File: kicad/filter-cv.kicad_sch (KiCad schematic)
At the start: 21 parts, among them Q10 2N3904, Q11 2N3906, Q9 2N3906, U16 TL074

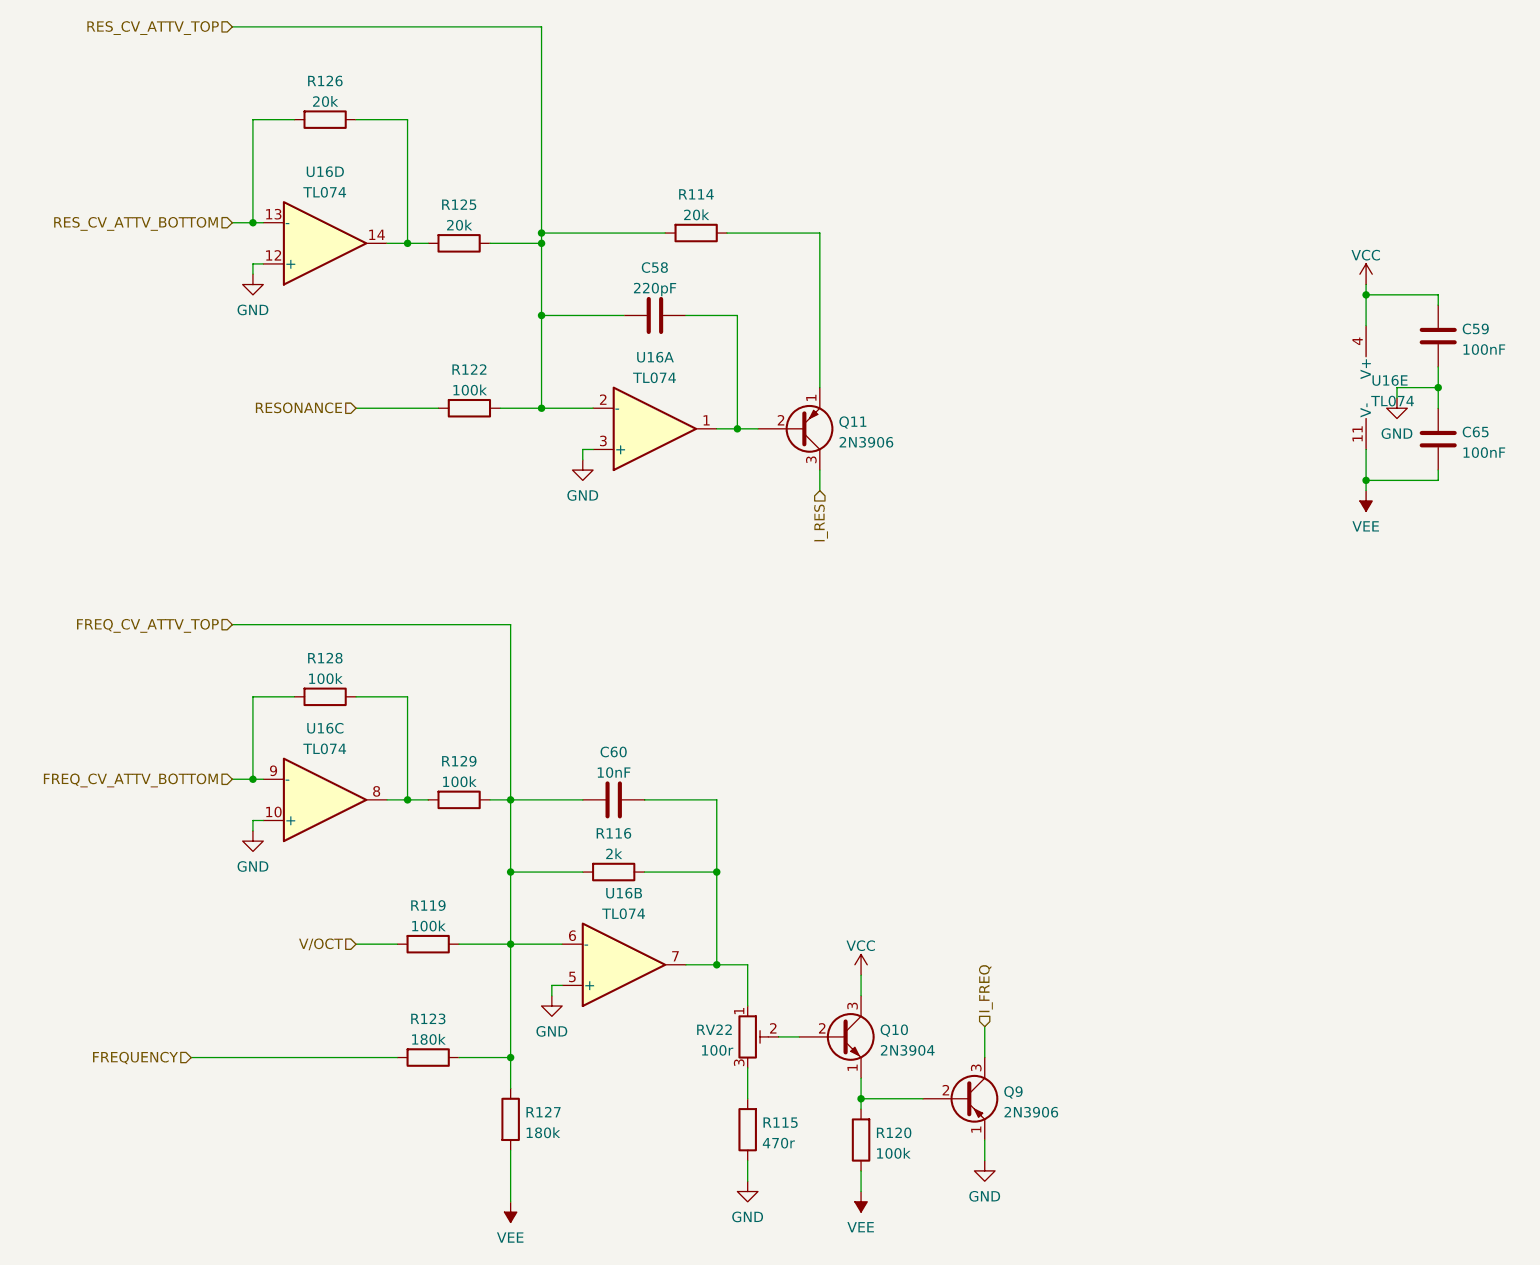
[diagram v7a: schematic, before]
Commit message: Updating for kicad 7
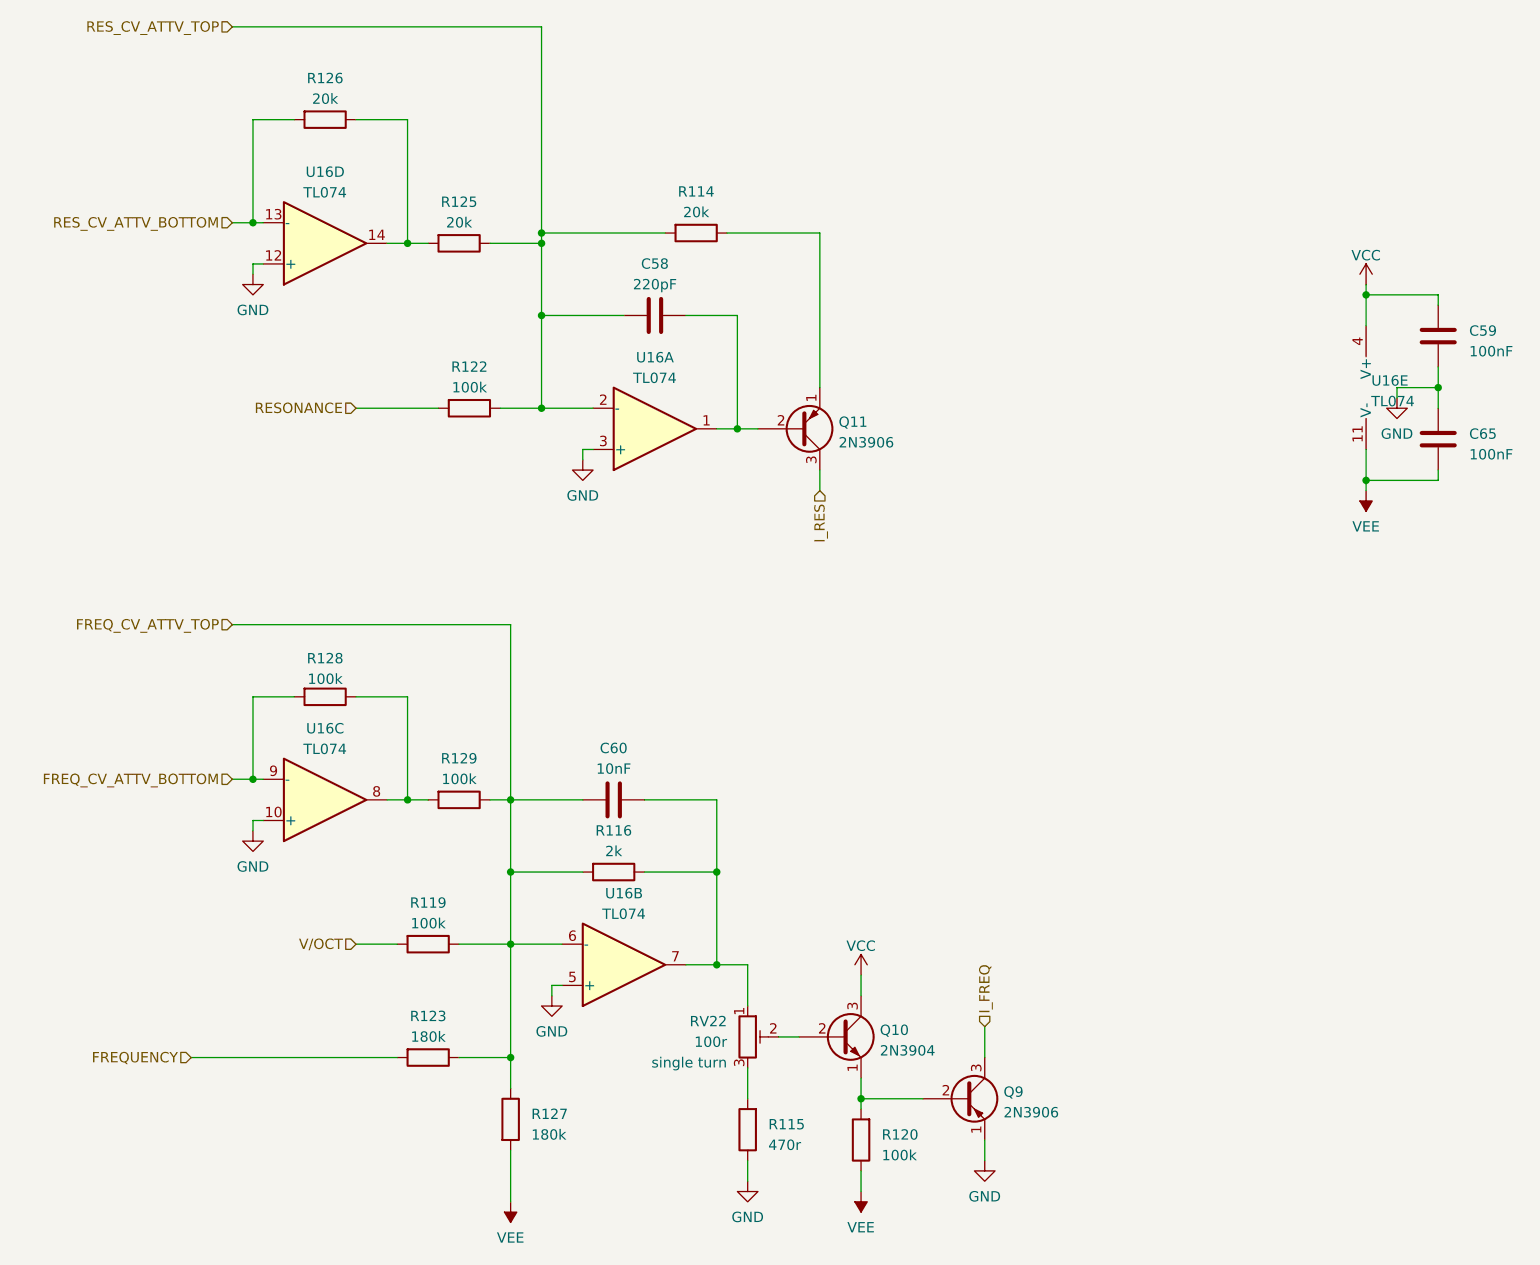
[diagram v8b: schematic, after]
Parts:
- C58, C60: footprint rumblesan-standard-parts:C_Rect_L7.0mm_W2.5mm_P5.00mm -> Rumblesan_Standard_Parts:C_Rect_L7.0mm_W2.5mm_P5.00mm; symbol rumblesan-standard-parts:C -> Rumblesan Standard Parts:C
- C59, C65: footprint rumblesan-standard-parts:C_Rect_L7.0mm_W2.5mm_P5.00mm -> Rumblesan_Standard_Parts:C_Rect_L7.0mm_W2.5mm_P5.00mm; symbol rumblesan-standard-parts:C -> Rumblesan Standard Parts:C; Spec ceramic X7R -> ceramic C0G
- Q10, Q11, Q9: footprint rumblesan-standard-parts:TO-92_Inline_Wide -> Rumblesan_Standard_Parts:TO-92_Inline_Wide
- R114, R115, R116, R119, R120, R122, R123, R125, R126, R127, R128, R129: footprint rumblesan-standard-parts:R_Axial_DIN0207_L6.3mm_D2.5mm_P10.16mm_Horizontal -> Rumblesan_Standard_Parts:R_Axial_DIN0207_L6.3mm_D2.5mm_P10.16mm_Horizontal; symbol rumblesan-standard-parts:R -> Rumblesan Standard Parts:R
- RV22: footprint rumblesan-standard-parts:Potentiometer_THT_Bourns_3306P_Vertical -> Rumblesan_Standard_Parts:Potentiometer_THT_Bourns_3306P_Vertical; symbol rumblesan-standard-parts:R_Potentiometer_Trim -> Rumblesan Standard Parts:R_Potentiometer_Trim
- U16: footprint rumblesan-standard-parts:DIP-14_W7.62mm_Socket -> Rumblesan_Standard_Parts:DIP-14_W7.62mm_Socket
